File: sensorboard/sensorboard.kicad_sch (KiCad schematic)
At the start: 63 parts, among them J10 Conn_01x02_Male, J11 Conn_01x05_Male, J15 Conn_Coaxial, J9 Conn_01x02_Male, Q1 MMDT2222A, U1 ESP32-PICO-D4, U2 LTC4411, U3 TPS61092RSAR

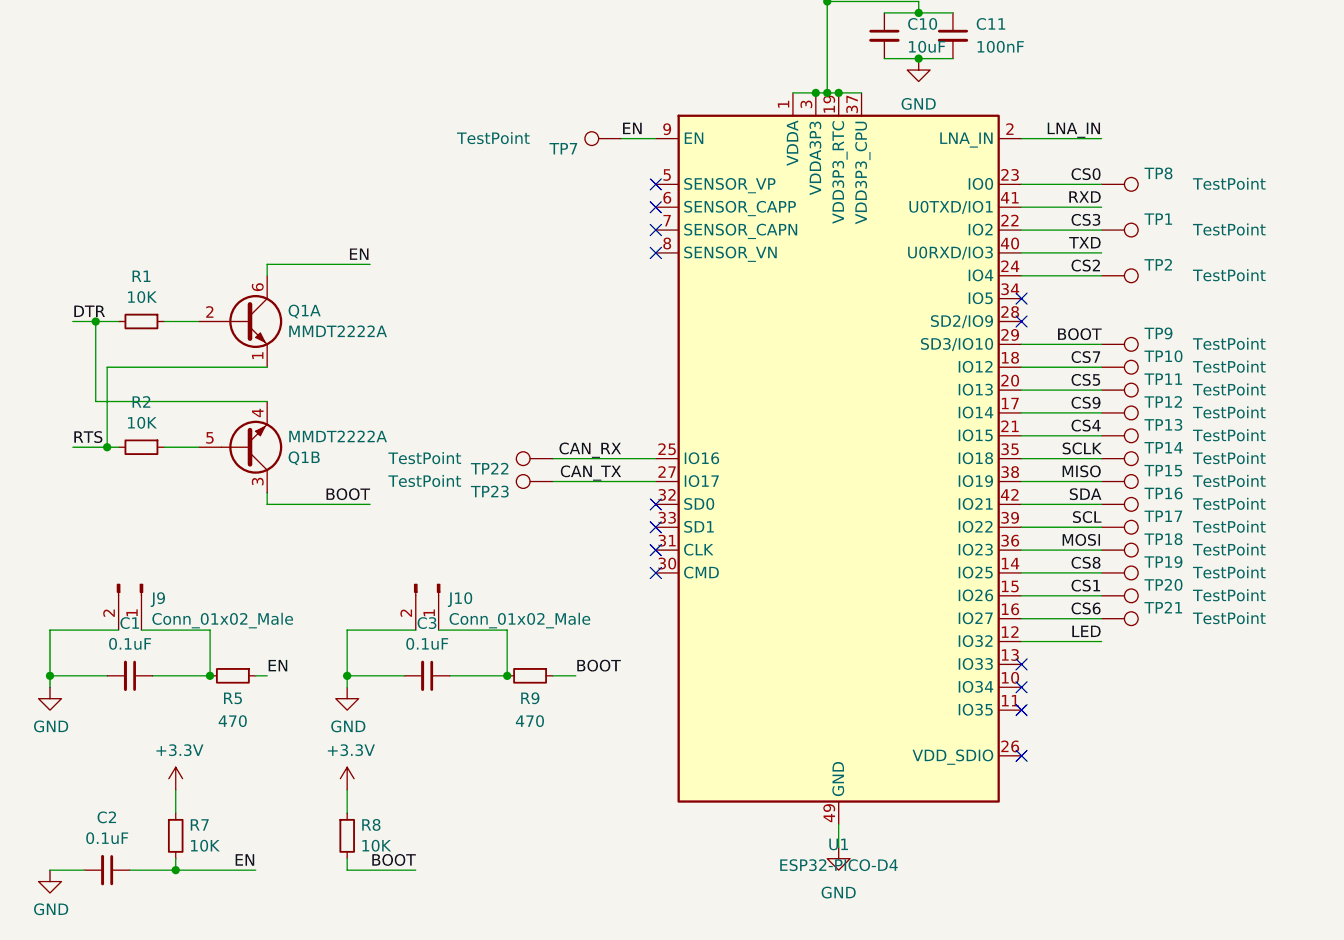
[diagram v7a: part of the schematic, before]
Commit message: changed BOOT pin, auto reset caps
moved references about
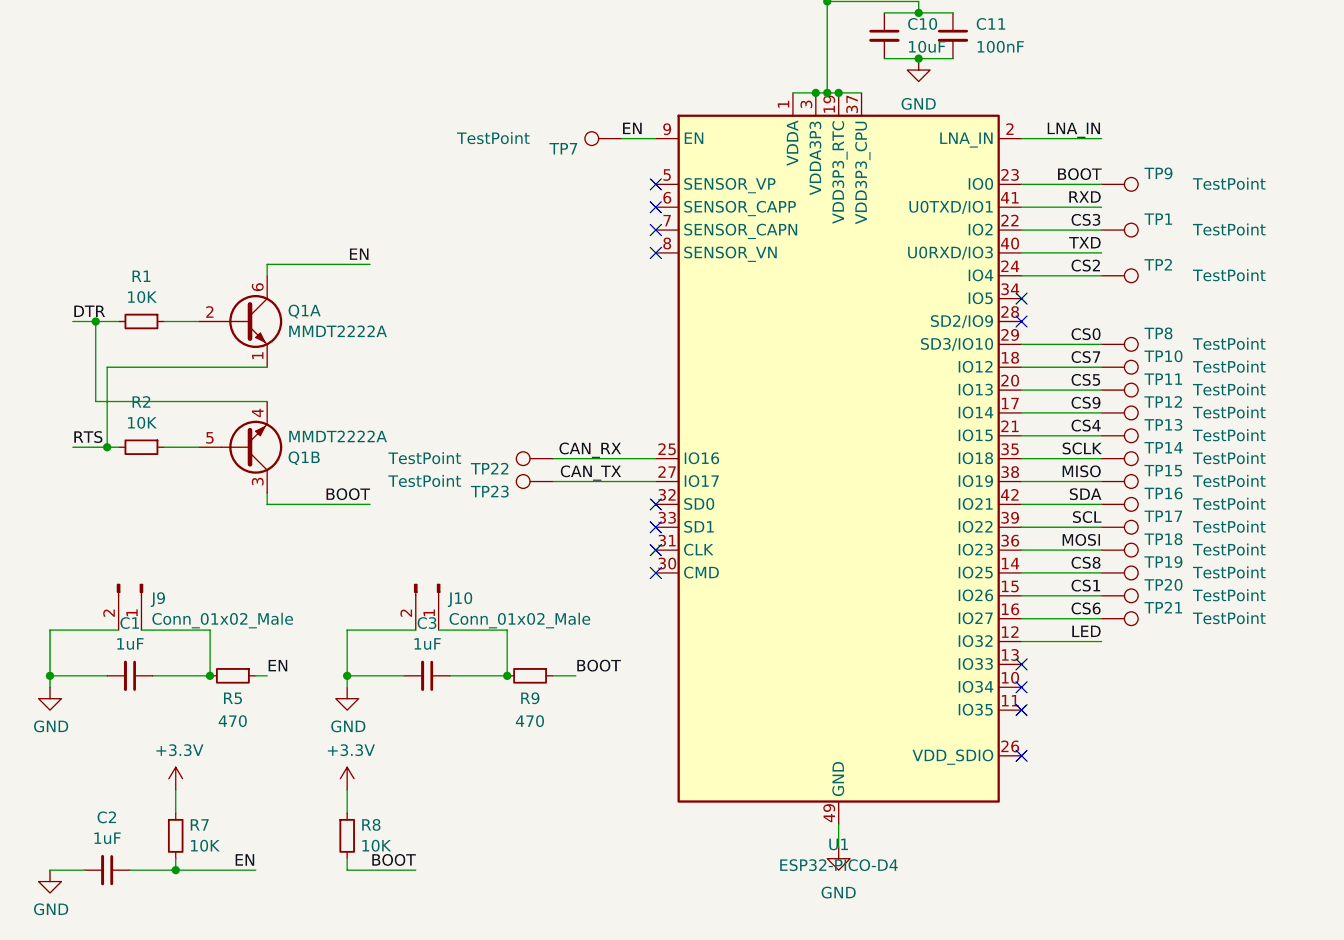
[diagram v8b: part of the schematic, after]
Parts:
- C1, C2, C3: value 0.1uF -> 1uF
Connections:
- net BOOT: now also U1.23 (IO0); no longer U1.29 (SD3/IO10)
- net CS0: now also U1.29 (SD3/IO10); no longer U1.23 (IO0)
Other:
- moved on the sheet: TP8, TP9
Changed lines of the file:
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@@
     (stroke (width 0) (type default) (color 0 0 0 0))
   )
+  (wire (pts (xy 124.46 133.35) (xy 133.35 133.35))
+    (stroke (width 0) (type default) (color 0 0 0 0))
+  )
   (wire (pts (xy 16.51 191.77) (xy 20.32 191.77))
     (stroke (width 0) (type default) (color 0 0 0 0))
@@
     (stroke (width 0) (type default) (color 0 0 0 0))
   )
-  (wire (pts (xy 124.46 115.57) (xy 133.35 115.57))
-    (stroke (width 0) (type default) (color 0 0 0 0))
-  )
   (wire (pts (xy 226.06 97.79) (xy 232.41 97.79))
     (stroke (width 0) (type default) (color 0 0 0 0))
@@
     (stroke (width 0) (type default) (color 0 0 0 0))
   )
+  (wire (pts (xy 124.46 115.57) (xy 133.35 115.57))
+    (stroke (width 0) (type default) (color 0 0 0 0))
+  )
   (wire (pts (xy 133.35 153.67) (xy 124.46 153.67))
     (stroke (width 0) (type default) (color 0 0 0 0))
@@
     (stroke (width 0) (type default) (color 0 0 0 0))
   )
-  (wire (pts (xy 124.46 133.35) (xy 133.35 133.35))
-    (stroke (width 0) (type default) (color 0 0 0 0))
-  )
   (wire (pts (xy 40.64 124.46) (xy 52.07 124.46))
     (stroke (width 0) (type default) (color 0 0 0 0))
@@
     (effects (font (size 1.27 1.27)) (justify right bottom))
   )
-  (label "BOOT" (at 133.35 133.35 180)
+  (label "BOOT" (at 133.35 115.57 180)
     (effects (font (size 1.27 1.27)) (justify right bottom))
   )
@@
     (effects (font (size 1.27 1.27)) (justify left bottom))
   )
-  (label "CS0" (at 133.35 115.57 180)
+  (label "CS0" (at 133.35 133.35 180)
     (effects (font (size 1.27 1.27)) (justify right bottom))
   )
@@
     (in_bom yes) (on_board yes)
     (property "Reference" "C2" (id 0) (at 22.86 185.9534 90))
-    (property "Value" "0.1uF" (id 1) (at 22.86 188.2648 90))
+    (property "Value" "1uF" (id 1) (at 22.86 188.2648 90))
     (property "Footprint" "Capacitor_SMD:C_0603_1608Metric" (id 2) (at 22.86 191.77 0)
       (effects (font (size 1.27 1.27)) hide)
@@
     (in_bom yes) (on_board yes)
     (property "Reference" "C3" (id 0) (at 58.42 164.3634 90))
-    (property "Value" "0.1uF" (id 1) (at 58.42 166.6748 90))
+    (property "Value" "1uF" (id 1) (at 58.42 166.6748 90))
     (property "Footprint" "Capacitor_SMD:C_0603_1608Metric" (id 2) (at 58.42 170.18 0)
       (effects (font (size 1.27 1.27)) hide)
@@
     (in_bom yes) (on_board yes)
     (property "Reference" "C1" (id 0) (at 25.4 164.3634 90))
-    (property "Value" "0.1uF" (id 1) (at 25.4 166.6748 90))
+    (property "Value" "1uF" (id 1) (at 25.4 166.6748 90))
     (property "Footprint" "Capacitor_SMD:C_0603_1608Metric" (id 2) (at 25.4 170.18 0)
       (effects (font (size 1.27 1.27)) hide)
@@
     (pin "1")
   )
-  (symbol (lib_id "Connector:TestPoint") (at 133.35 133.35 270) (unit 1)
+  (symbol (lib_id "Connector:TestPoint") (at 133.35 115.57 270) (unit 1)
     (in_bom yes) (on_board yes)
-    (property "Reference" "TP9" (id 0) (at 138.1252 132.1816 90)
+    (property "Reference" "TP9" (id 0) (at 138.1252 114.4016 90)
       (effects (font (size 1.27 1.27)) (justify left))
     )
-    (property "Value" "TestPoint" (id 1) (at 143.51 133.35 90)
+    (property "Value" "TestPoint" (id 1) (at 143.51 115.57 90)
       (effects (font (size 1.27 1.27)) (justify left))
     )
-    (property "Footprint" "TestPoint:TestPoint_Pad_D1.0mm" (id 2) (at 133.35 138.43 0)
+    (property "Footprint" "TestPoint:TestPoint_Pad_D1.0mm" (id 2) (at 133.35 120.65 0)
       (effects (font (size 1.27 1.27)) hide)
     )
-    (property "Datasheet" "~" (id 3) (at 133.35 138.43 0)
+    (property "Datasheet" "~" (id 3) (at 133.35 120.65 0)
       (effects (font (size 1.27 1.27)) hide)
     )
@@
     (pin "1")
   )
-  (symbol (lib_id "Connector:TestPoint") (at 133.35 115.57 270) (unit 1)
+  (symbol (lib_id "Connector:TestPoint") (at 133.35 133.35 270) (unit 1)
     (in_bom yes) (on_board yes)
-    (property "Reference" "TP8" (id 0) (at 138.1252 114.4016 90)
+    (property "Reference" "TP8" (id 0) (at 138.1252 132.1816 90)
       (effects (font (size 1.27 1.27)) (justify left))
     )
-    (property "Value" "TestPoint" (id 1) (at 143.51 115.57 90)
+    (property "Value" "TestPoint" (id 1) (at 143.51 133.35 90)
       (effects (font (size 1.27 1.27)) (justify left))
     )
-    (property "Footprint" "TestPoint:TestPoint_Pad_D1.0mm" (id 2) (at 133.35 120.65 0)
+    (property "Footprint" "TestPoint:TestPoint_Pad_D1.0mm" (id 2) (at 133.35 138.43 0)
       (effects (font (size 1.27 1.27)) hide)
     )
-    (property "Datasheet" "~" (id 3) (at 133.35 120.65 0)
+    (property "Datasheet" "~" (id 3) (at 133.35 138.43 0)
       (effects (font (size 1.27 1.27)) hide)
     )
@@
     )
     (path "/00000000-0000-0000-0000-00005dabbfe7"
-      (reference "C1") (unit 1) (value "0.1uF") (footprint "Capacitor_SMD:C_0603_1608Metric")
+      (reference "C1") (unit 1) (value "1uF") (footprint "Capacitor_SMD:C_0603_1608Metric")
     )
     (path "/00000000-0000-0000-0000-00005da70d8a"
-      (reference "C2") (unit 1) (value "0.1uF") (footprint "Capacitor_SMD:C_0603_1608Metric")
+      (reference "C2") (unit 1) (value "1uF") (footprint "Capacitor_SMD:C_0603_1608Metric")
     )
     (path "/00000000-0000-0000-0000-00005dab5946"
-      (reference "C3") (unit 1) (value "0.1uF") (footprint "Capacitor_SMD:C_0603_1608Metric")
+      (reference "C3") (unit 1) (value "1uF") (footprint "Capacitor_SMD:C_0603_1608Metric")
     )
     (path "/00000000-0000-0000-0000-000061cb93b1/00000000-0000-0000-0000-00006199d7ef"
@@
       (reference "R66") (unit 1) (value "47k") (footprint "Resistor_SMD:R_0603_1608Metric")
     )
-    (path "/a190bd03-a44f-406d-b509-db6d2721c035/6b108607-8b3c-4b71-8117-4209ede9078e"
-      (reference "R67") (unit 1) (value "90") (footprint "Resistor_SMD:R_0603_1608Metric")
-    )
-    (path "/a190bd03-a44f-406d-b509-db6d2721c035/7d2e508b-7d76-4b84-a3b0-f1fb0741f189"
-      (reference "R68") (unit 1) (value "90") (footprint "Resistor_SMD:R_0603_1608Metric")
-    )
     (path "/a190bd03-a44f-406d-b509-db6d2721c035/523026c1-1e6c-4bdd-9348-ee3536bc5a61"
       (reference "R69") (unit 1) (value "10k") (footprint "Resistor_SMD:R_0603_1608Metric")
     )
     (path "/a190bd03-a44f-406d-b509-db6d2721c035/67893643-a821-4fb9-a047-23ff68e41f23"
-      (reference "R70") (unit 1) (value "60") (footprint "Resistor_SMD:R_0805_2012Metric")
+      (reference "R70") (unit 1) (value "60") (footprint "Resistor_SMD:R_0603_1608Metric")
     )
     (path "/a190bd03-a44f-406d-b509-db6d2721c035/dec4d9c9-fa16-4cbf-b380-1853d63351e5"
-      (reference "R71") (unit 1) (value "60") (footprint "Resistor_SMD:R_0805_2012Metric")
+      (reference "R71") (unit 1) (value "60") (footprint "Resistor_SMD:R_0603_1608Metric")
     )
     (path "/00000000-0000-0000-0000-000061cb93b1/00000000-0000-0000-0000-00006199b0f6"
